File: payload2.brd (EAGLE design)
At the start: 100 x 80 mm, 26 parts, among them U1 ATMEGA328P_TQFP, U2 USD-SOCKETSMD, U3 3.3V/150mA, U4 9DoF IMU, Y1 16MHz

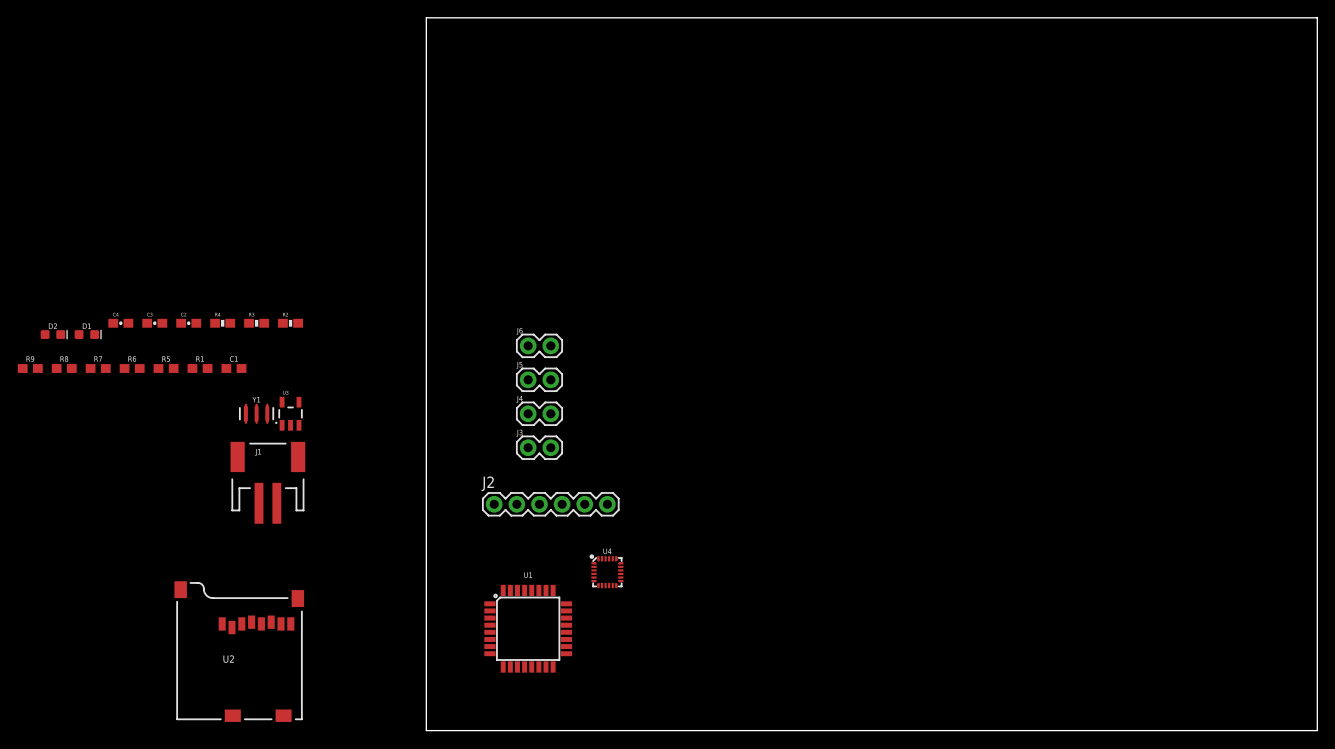
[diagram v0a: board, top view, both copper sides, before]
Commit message: Started moving components in board file
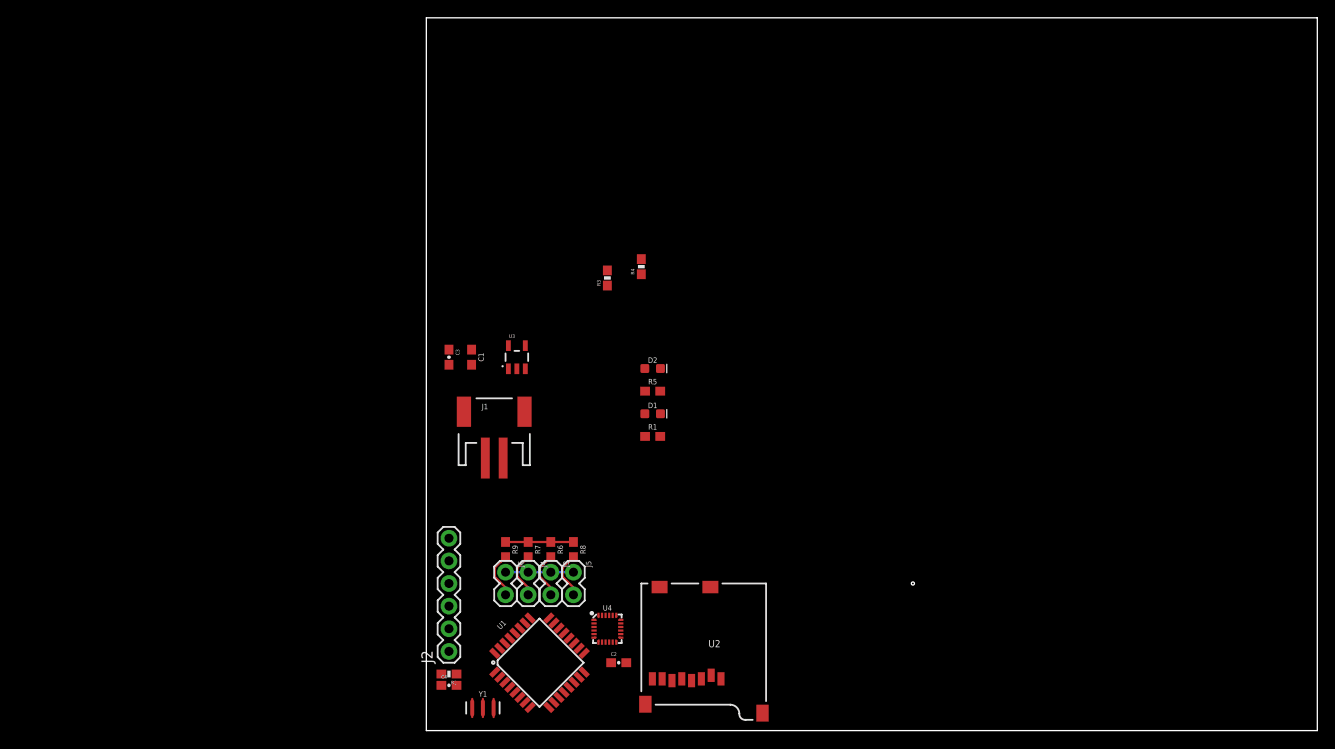
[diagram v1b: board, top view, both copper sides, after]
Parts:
- moved D2 67.4 mm to (25.4, 40.6)
- moved D1 64.1 mm to (25.4, 35.6)
- moved C2 61.5 mm to (21.6, 7.62)
- moved R8 60.7 mm to (16.5, 20.3), turned to 270 degrees
- moved R9 57.1 mm to (8.89, 20.3), turned to 270 degrees
- moved C4 54.8 mm to (2.54, 5.08)
- moved R5 54.7 mm to (25.4, 38.1)
- moved R7 52.4 mm to (11.4, 20.3), turned to 270 degrees
- moved R1 51.4 mm to (25.4, 33.0)
- moved R6 51.2 mm to (14.0, 20.3), turned to 270 degrees
- moved R4 47.4 mm to (24.1, 52.1), turned to 90 degrees
- moved R2 43.2 mm to (2.54, 6.35), turned to 180 degrees
- moved Y1 41.7 mm to (6.35, 2.54)
- moved U2 41.0 mm to (24.1, 16.5), turned to 180 degrees
- moved R3 39.7 mm to (20.3, 50.8), turned to 90 degrees
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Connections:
- net N$11 renamed XTAL2
- net N$8 renamed IO5
- net N$9 renamed XTAL1
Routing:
- net GND: track 0.00 -> 7.62 mm
- net 3.3V: track 0.00 -> 7.62 mm
- net A0: track 0.00 -> 5.26 mm
- net A3: track 0.00 -> 5.26 mm
- net A1: track 0.00 -> 5.26 mm
- net A2: track 0.00 -> 5.26 mm

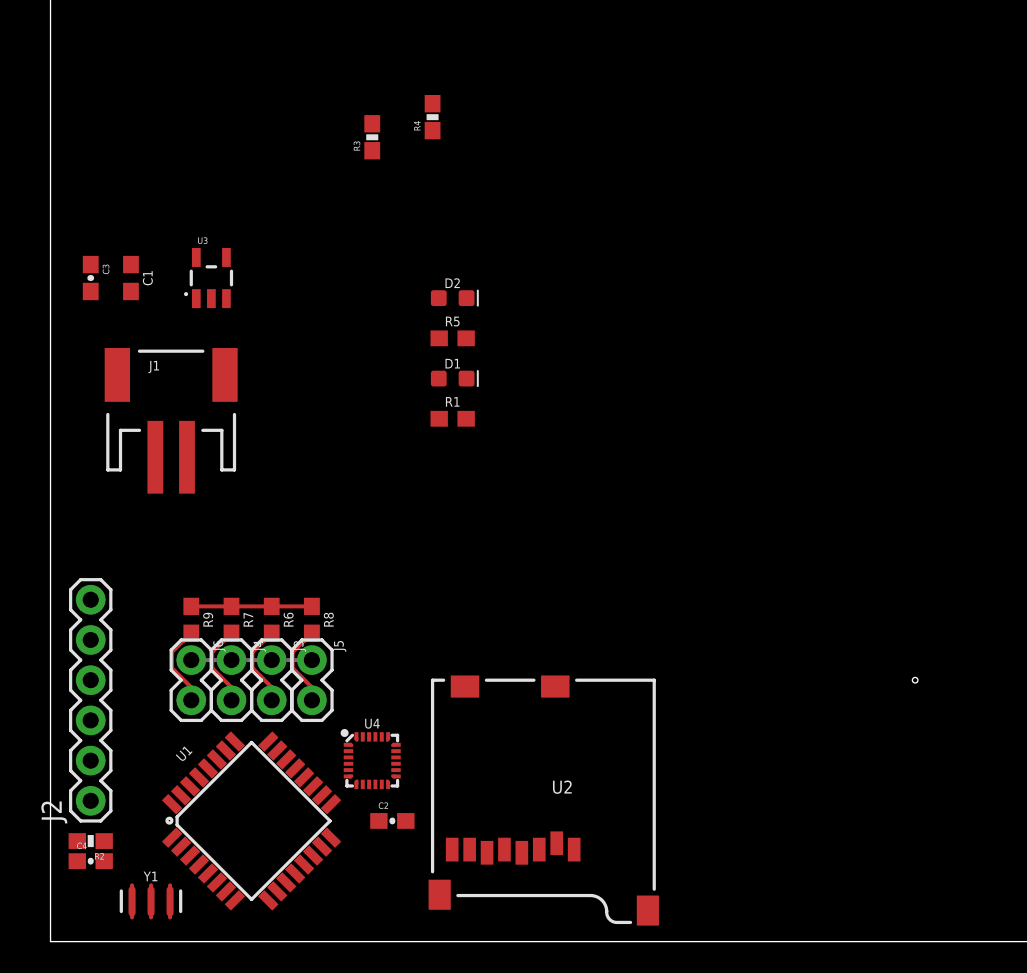
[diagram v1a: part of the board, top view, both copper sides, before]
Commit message: Worked on routing on board file.  Added screw switch connectors.
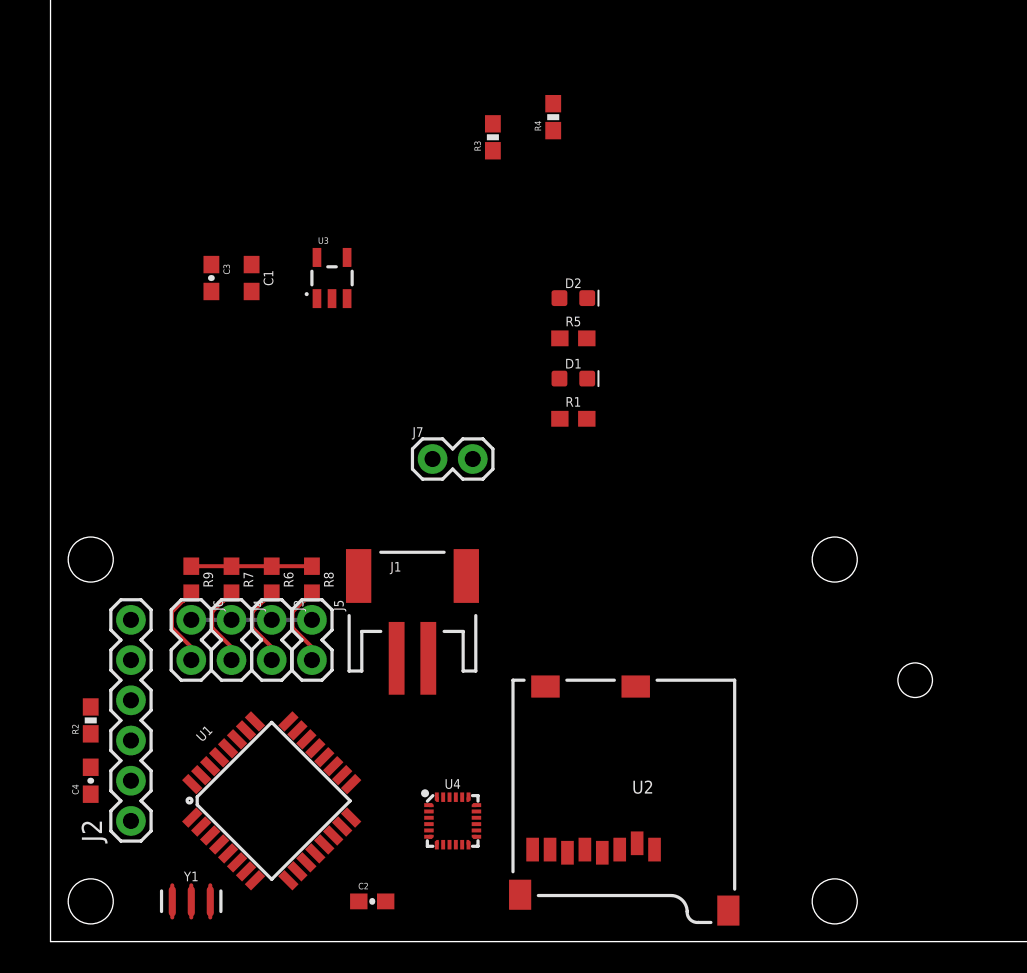
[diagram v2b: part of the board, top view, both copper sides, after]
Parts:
- added J7: (no value), SparkFun-Connectors:1X02
- moved J1 19.8 mm to (22.9, 21.6)
- moved D1 7.62 mm to (33.0, 35.6)
- moved D2 7.62 mm to (33.0, 40.6)
- moved R1 7.62 mm to (33.0, 33.0)
- moved R5 7.62 mm to (33.0, 38.1)
- moved R2 7.62 mm to (2.54, 14.0), turned to 90 degrees
- moved R3 7.62 mm to (27.9, 50.8)
- moved R4 7.62 mm to (31.8, 52.1)
- moved U3 7.62 mm to (17.8, 41.9)
- moved C3 7.62 mm to (10.2, 41.9)
- moved C1 7.62 mm to (12.7, 41.9)
- moved U4 6.35 mm to (25.4, 7.62)
- moved C2 5.24 mm to (20.3, 2.54)
- moved U2 5.08 mm to (29.2, 16.5)
- moved C4 5.08 mm to (2.54, 10.2), turned to 90 degrees
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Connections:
- new net N$1: J1.2, J7.2
- net N$4: now also J7.1; no longer J1.2

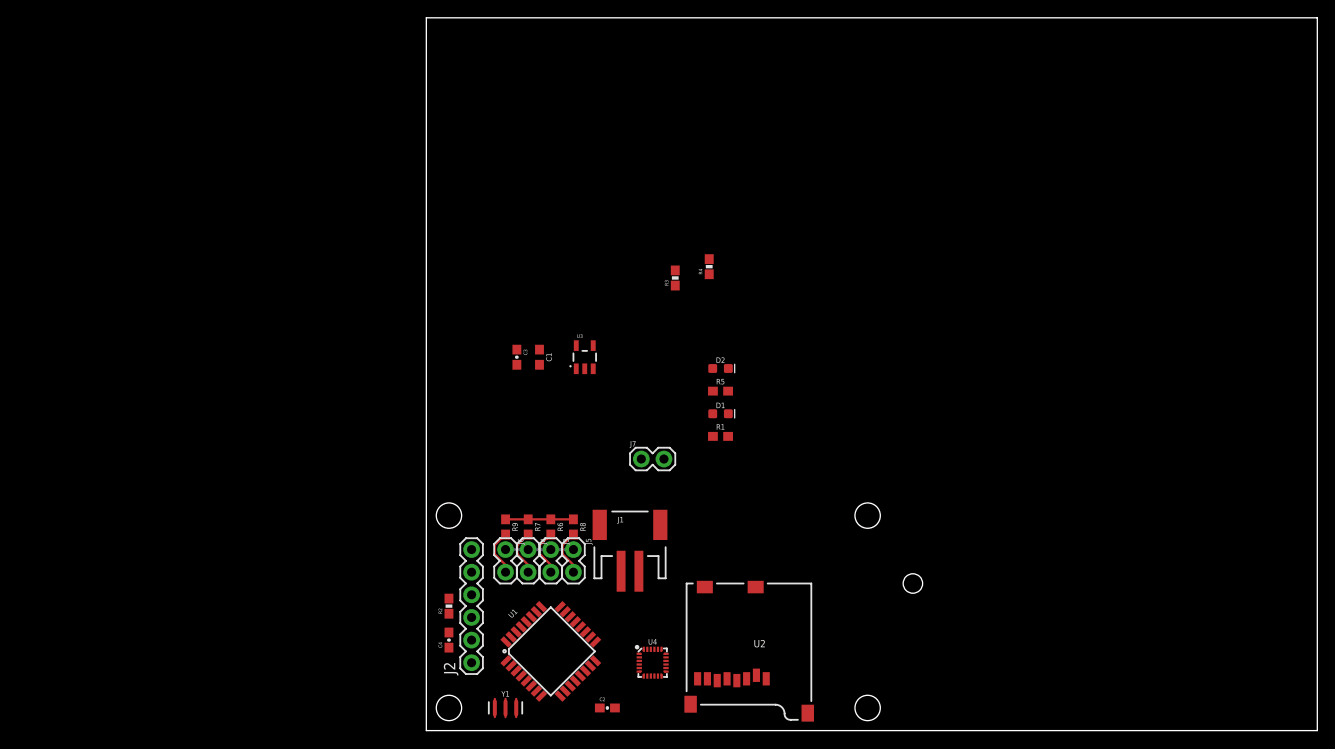
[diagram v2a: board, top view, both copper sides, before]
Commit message: Finalized board design.  Worked screw sizes and possitioning.  Switched two hole connector for battery connector.  added jumpers for battery charger.
Board should be ready to order.  Things that still need to improve:
1) final check and look over.
2) silk screen could be improved.
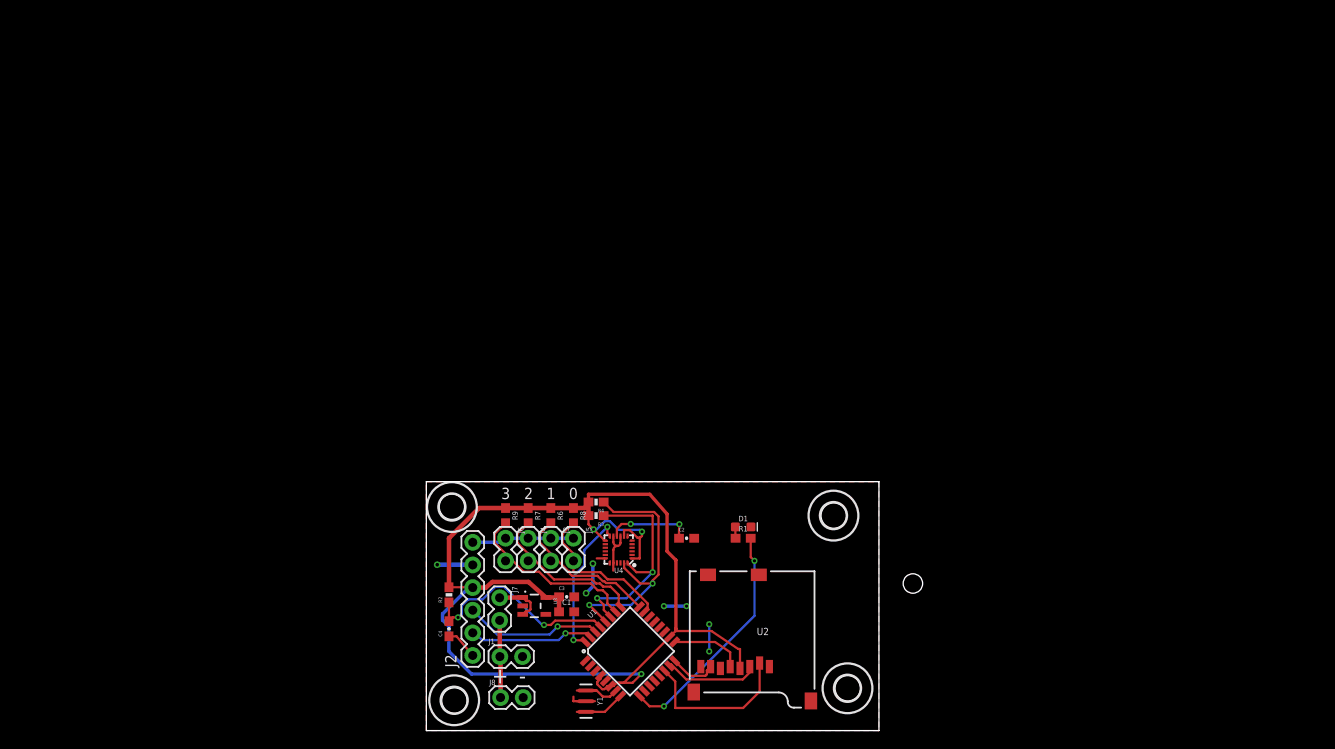
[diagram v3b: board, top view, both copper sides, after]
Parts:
- removed D2: RED, femtosat:LED-0603
- removed R5: 330, femtosat:0603
- added J8: (no value), SparkFun-Connectors:1X02
- J1: device femtosat:JST-2-SMD -> SparkFun-Connectors:1X02
- moved R4 29.3 mm to (19.1, 25.7), turned to 180 degrees
- moved C1 28.7 mm to (15.7, 13.3), turned to 0 degrees
- moved U3 28.5 mm to (12.1, 14.0), turned to 270 degrees
- moved R3 28.1 mm to (19.1, 24.1), turned to 180 degrees
- moved C3 27.5 mm to (15.7, 15.0), turned to 0 degrees
- moved J7 22.3 mm to (8.23, 14.9), turned to 270 degrees
- moved C2 21.0 mm to (29.2, 21.6)
- moved J1 19.7 mm to (8.26, 8.31)
- moved U4 13.3 mm to (21.6, 20.3), turned to 180 degrees
- moved D1 13.0 mm to (35.6, 22.9)
- moved R1 11.7 mm to (35.6, 21.6)
- moved Y1 9.05 mm to (17.9, 3.30), turned to 270 degrees
- moved U1 8.89 mm to (22.9, 8.89)
- moved U2 1.42 mm to (29.6, 17.9)
- moved C4 1.27 mm to (2.54, 11.4)
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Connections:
- removed net N$1: J1.2, J7.2
- removed net N$10: D2.A, R5.1
- new net VIN: J1.1, J7.2, J8.1
- net 3.3V: no longer R5.2
- net GND: now also J1.2, J8.2; no longer D2.C, J1.1
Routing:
- net 3.3V: track 7.62 -> 138.7 mm, vias 0 -> 3
- net SCL: track 0.00 -> 29.9 mm, vias 0 -> 2
- net IO5: track 0.00 -> 26.5 mm, vias 0 -> 2
- net GND: track 7.62 -> 33.0 mm, vias 0 -> 7
- net SDA: track 0.00 -> 25.2 mm, vias 0 -> 2
- net RESET: track 0.00 -> 23.5 mm, vias 0 -> 2
- net SS: track 0.00 -> 18.1 mm
- net INT: track 0.00 -> 16.9 mm, vias 0 -> 2
- net RXD: track 0.00 -> 15.5 mm, vias 0 -> 1
- net A3: track 5.26 -> 20.5 mm
- net TXD: track 0.00 -> 13.9 mm, vias 0 -> 1
- net A2: track 5.26 -> 18.4 mm
- net A1: track 5.26 -> 17.4 mm
- net A0: track 5.26 -> 17.4 mm
- net MOSI: track 0.00 -> 10.7 mm
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- added copper zone on layer 1, net GND
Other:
- board size 100 x 80 mm -> 50.8 x 27.9 mm
- board text added: "+"
- board text added: "-"
- board text added: "0"
- board text added: "1"
- board text added: "2"
- board text added: "3"
